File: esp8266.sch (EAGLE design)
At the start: 31 parts, among them U1 FT232RL-BASICSSOP, U2 SPX3819M5-L33, U3 SPX3819M5-L33

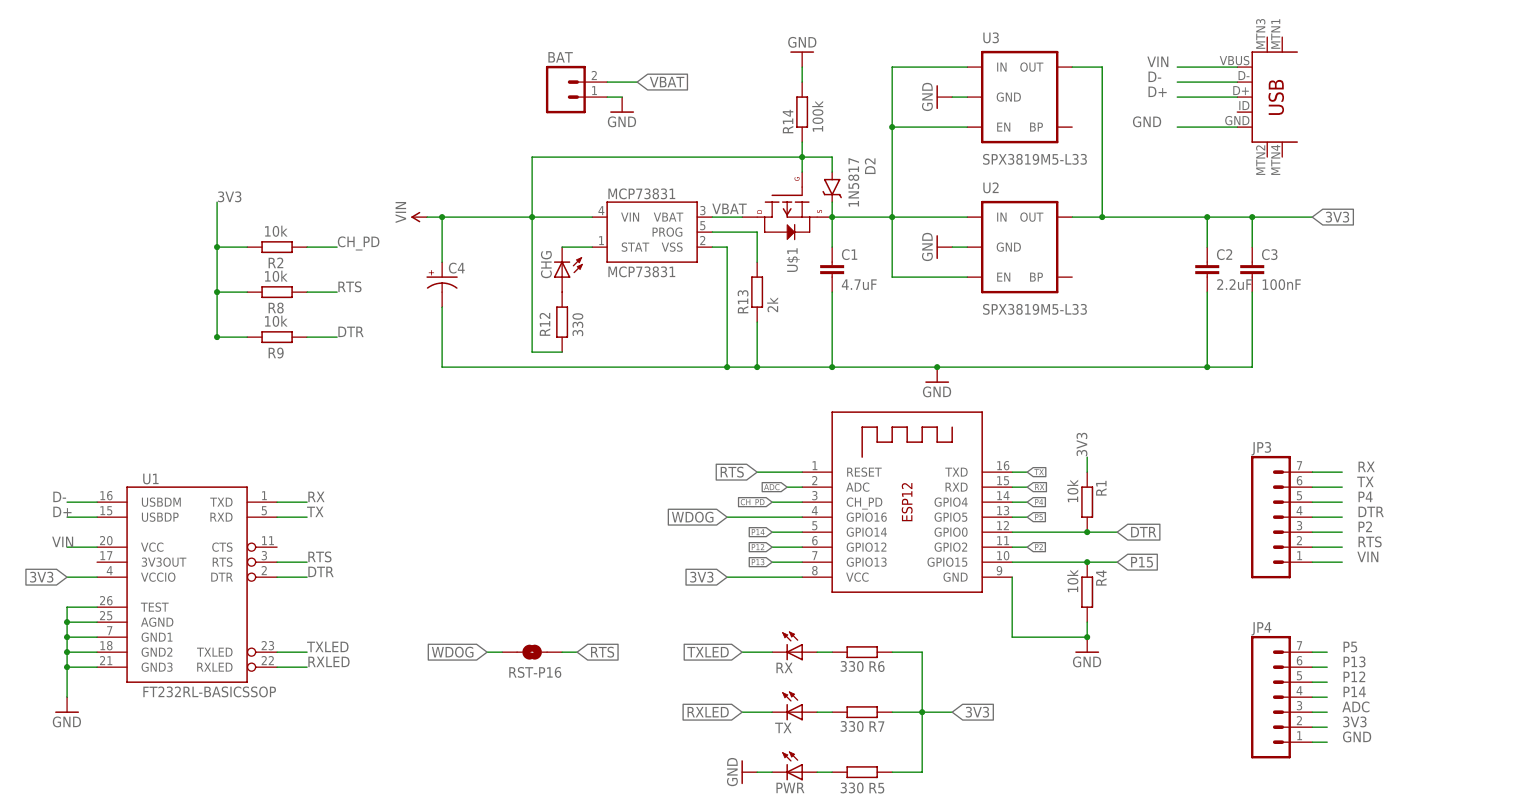
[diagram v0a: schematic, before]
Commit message: Minor fixes and improvements.
Watchdog with pull ups and a AND Gate;
Diode after VIN for satefy reasons;
Additional VIN pin on the other side of the board for completeness;
Switched order of pins 13 and 12;
Small border test holes for VIN and GND.
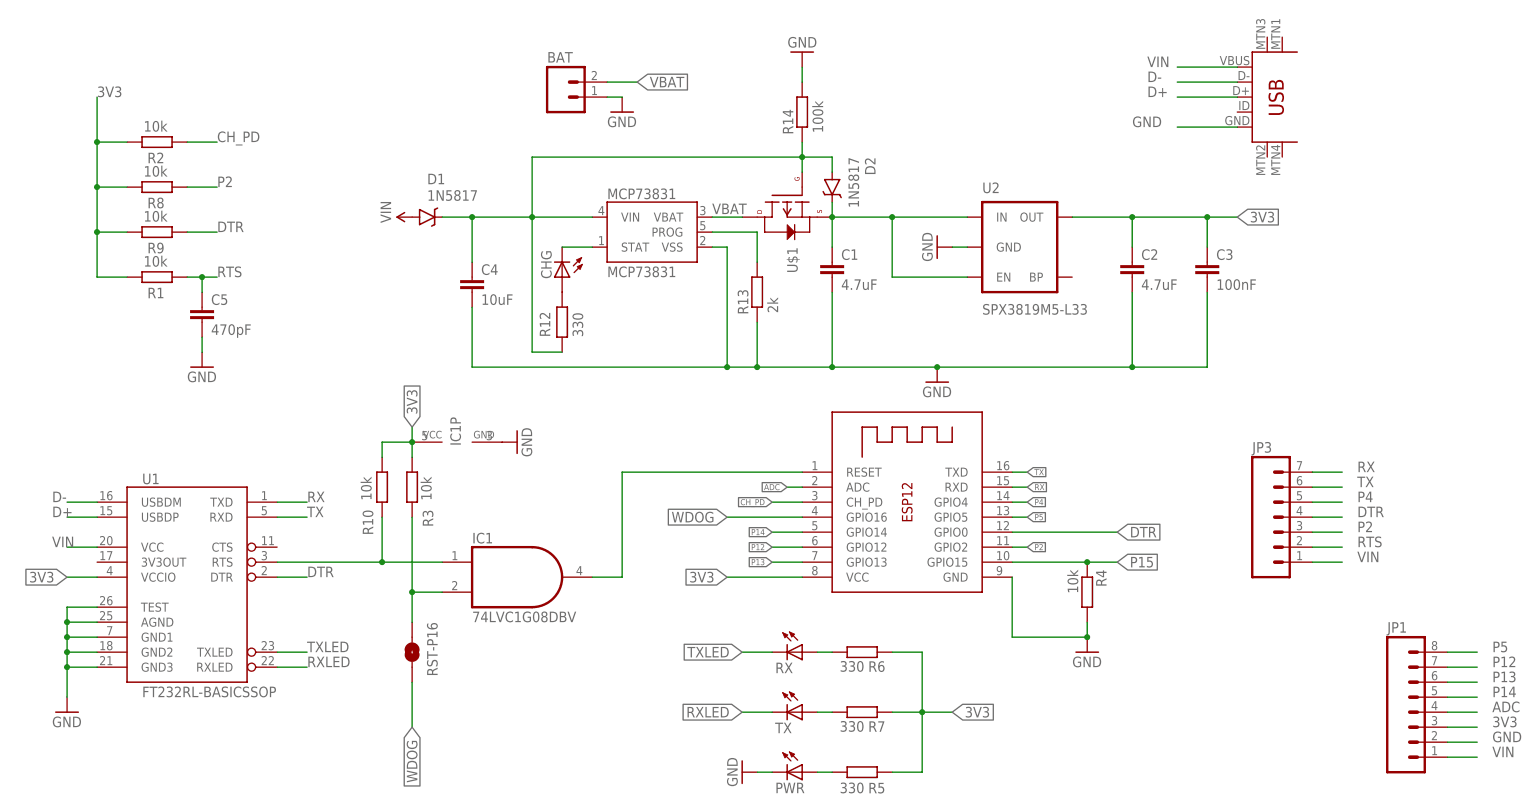
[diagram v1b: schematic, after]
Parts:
- removed JP4: (no value), SparkFun-Connectors:M07LOCK
- removed U3: SPX3819M5-L33, SparkFun-PowerIC:V_REG_LDOSMD
- added C5: 470pF, rcl:C-EUC0805
- added D1: 1N5817, SparkFun-DiscreteSemi:DIODE-SCHOTTKY-MBRA140
- added IC1: 74LVC1G08DBV, 74xx-little-us:74LVC1G08DBV
- added JP1: (no value), SparkFun-Connectors:M08LOCK
- added R10, R3: 10k, resistor:R-EU_R0805
- C2: value 2.2uF -> 4.7uF
- C4: value (none) -> 10uF; device SparkFun-Capacitors:CAP_POL1206 -> rcl:C-EUC0805
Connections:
- new net FTDI_RTS: IC1A.I0, R10.1, U1.RTS
- new net N$2: C4.1, D1.C, D2.A, MCP73831.VIN, R12.1, R14.1, U$1.G
- new net N$4: IC1A.I1, R3.1, RST-P16.1
- net 3V3: now also IC1P.VCC, JP1.3, R10.2, R3.2; no longer JP4.2, U3.OUT
- net ADC: now also JP1.4; no longer JP4.3
- net DTR: no longer R1.2
- net GND: now also C4.2, C5.2, IC1P.GND, JP1.2; no longer C4.-, JP4.1, U3.GND
- net P12: now also JP1.7; no longer JP4.5
- net P13: now also JP1.6; no longer JP4.6
- net P14: now also JP1.5; no longer JP4.4
- net P2: now also R8.2
- net P5: now also JP1.8; no longer JP4.7
- net RTS: now also C5.1, IC1A.O, R1.2; no longer R8.2, RST-P16.1, U1.RTS
- net VIN: now also D1.A, JP1.1; no longer C4.+, D2.A, MCP73831.VIN, R12.1, R14.1, U$1.G
- net VRIN: no longer U3.EN, U3.IN
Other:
- moved on the sheet: C2, C3, R1, R2, R8, R9, RST-P16

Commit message: Remove unnecessary components
RTS had a capacitor that is not required per FTDI spec and is also not needed for this
circuit. There were also 2 10k pull-ups on the RTS.
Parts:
- removed C5: 470pF, rcl:C-EUC0805
- removed R1: 10k, resistor:R-EU_R0805
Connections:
- net 3V3: no longer R1.1
- net GND: no longer C5.2
- net RTS: no longer C5.1, R1.2
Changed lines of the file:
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@@
 <part name="U2" library="SparkFun-PowerIC" deviceset="V_REG_LDO" device="SMD" value="SPX3819M5-L33"/>
 <part name="GND1" library="supply1" deviceset="GND" device=""/>
-<part name="R1" library="resistor" deviceset="R-EU_" device="R0805" value="10k"/>
-<part name="C5" library="rcl" deviceset="C-EU" device="C0805" value="470pF"/>
-<part name="GND9" library="supply1" deviceset="GND" device=""/>
 <part name="C4" library="rcl" deviceset="C-EU" device="C0805" value="10uF"/>
 <part name="D1" library="SparkFun-DiscreteSemi" deviceset="DIODE-SCHOTTKY" device="-MBRA140" value="1N5817"/>
@@
 </instance>
 <instance part="GND1" gate="1" x="27.94" y="109.22" rot="R270"/>
-<instance part="R1" gate="G$1" x="-104.14" y="104.14" smashed="yes">
-<attribute name="NAME" x="-102.87" y="102.3366" size="1.778" layer="95" rot="R180"/>
-<attribute name="VALUE" x="-102.362" y="107.696" size="1.778" layer="96" rot="R180"/>
-</instance>
-<instance part="C5" gate="G$1" x="-96.52" y="99.06"/>
-<instance part="GND9" gate="1" x="-96.52" y="88.9"/>
 <instance part="C4" gate="G$1" x="-50.8" y="104.14"/>
 <instance part="D1" gate="G$1" x="-58.42" y="114.3" smashed="yes">
@@
 </segment>
 <segment>
-<pinref part="C5" gate="G$1" pin="2"/>
-<wire x1="-96.52" y1="93.98" x2="-96.52" y2="91.44" width="0.1524" layer="91"/>
-<pinref part="GND9" gate="1" pin="GND"/>
-</segment>
-<segment>
 <pinref part="JP1" gate="G$1" pin="2"/>
 <wire x1="114.3" y1="25.4" x2="119.38" y2="25.4" width="0.1524" layer="91"/>
@@
 <wire x1="91.44" y1="58.42" x2="96.52" y2="58.42" width="0.1524" layer="91"/>
 <label x="99.06" y="58.42" size="1.778" layer="95"/>
-</segment>
-<segment>
-<pinref part="R1" gate="G$1" pin="2"/>
-<wire x1="-99.06" y1="104.14" x2="-96.52" y2="104.14" width="0.1524" layer="91"/>
-<label x="-93.98" y="104.14" size="1.778" layer="95"/>
-<pinref part="C5" gate="G$1" pin="1"/>
-<wire x1="-96.52" y1="104.14" x2="-93.98" y2="104.14" width="0.1524" layer="91"/>
-<wire x1="-96.52" y1="101.6" x2="-96.52" y2="104.14" width="0.1524" layer="91"/>
-<junction x="-96.52" y="104.14"/>
 </segment>
 </net>
@@
 <junction x="-114.3" y="127"/>
 <junction x="-114.3" y="119.38"/>
-<junction x="-114.3" y="111.76"/>
-<pinref part="R1" gate="G$1" pin="1"/>
-<wire x1="-109.22" y1="104.14" x2="-114.3" y2="104.14" width="0.1524" layer="91"/>
-<wire x1="-114.3" y1="104.14" x2="-114.3" y2="111.76" width="0.1524" layer="91"/>
-</segment>
-<segment>
+</segment>
+<segment>

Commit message: Change the second VIN to ground
It's more useful that way.
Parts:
- added PFET2: BSS84, transistor-small-signal:BSS84
- renumbered U$1 to PFET1
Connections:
- new net N$5: BAT.1, PFET2.D
- net GND: now also BAT.2, JP3.1, PFET2.G; no longer BAT.1
- net VBAT: now also PFET2.S; no longer BAT.2
- net VIN: no longer JP3.1
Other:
- moved on the sheet: BAT
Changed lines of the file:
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@@
 <?xml version="1.0" encoding="utf-8"?>
 <!DOCTYPE eagle SYSTEM "eagle.dtd">
-<eagle version="7.3.0">
+<eagle version="7.4.0">
 <drawing>
 <settings>
@@
 <part name="BAT" library="SparkFun-Connectors" deviceset="M02" device="LOCK"/>
 <part name="SUPPLY1" library="SparkFun-Aesthetics" deviceset="VIN" device=""/>
-<part name="GND4" library="supply1" deviceset="GND" device=""/>
-<part name="U$1" library="GeekAmmo" deviceset="P-CHANNEL-MOSFET" device=""/>
+<part name="PFET1" library="GeekAmmo" deviceset="P-CHANNEL-MOSFET" device=""/>
 <part name="R14" library="resistor" deviceset="R-EU_" device="R0805" value="100k"/>
 <part name="GND6" library="supply1" deviceset="GND" device=""/>
@@
 <part name="JP1" library="SparkFun-Connectors" deviceset="M08" device="LOCK"/>
 <part name="GND7" library="supply1" deviceset="GND" device=""/>
+<part name="PFET2" library="transistor-small-signal" deviceset="BSS84" device=""/>
+<part name="GND4" library="supply1" deviceset="GND" device=""/>
 </parts>
 <sheets>
@@
 <attribute name="VALUE" x="1.016" y="98.044" size="1.778" layer="96" rot="R90"/>
 </instance>
-<instance part="BAT" gate="G$1" x="-35.56" y="134.62"/>
+<instance part="BAT" gate="G$1" x="-48.26" y="137.16"/>
 <instance part="SUPPLY1" gate="G$1" x="-60.96" y="114.3" rot="R90"/>
-<instance part="GND4" gate="1" x="-25.4" y="132.08"/>
-<instance part="U$1" gate="G$1" x="2.54" y="116.84" smashed="yes" rot="R270">
+<instance part="PFET1" gate="G$1" x="2.54" y="116.84" smashed="yes" rot="R270">
 <attribute name="NAME" x="2.54" y="109.22" size="1.778" layer="95" rot="R270"/>
 </instance>
@@
 <instance part="IC1" gate="P" x="-53.34" y="76.2" rot="R90"/>
 <instance part="GND7" gate="1" x="-43.18" y="76.2" rot="R90"/>
+<instance part="PFET2" gate="G$1" x="-30.48" y="137.16" rot="R270"/>
+<instance part="GND4" gate="1" x="-27.94" y="144.78" rot="R180"/>
 </instances>
 <busses>
@@
 </segment>
 <segment>
-<pinref part="BAT" gate="G$1" pin="1"/>
-<wire x1="-25.4" y1="134.62" x2="-27.94" y2="134.62" width="0.1524" layer="91"/>
-<pinref part="GND4" gate="1" pin="GND"/>
-</segment>
-<segment>
 <pinref part="GND6" gate="1" pin="GND"/>
 <pinref part="R14" gate="G$1" pin="2"/>
@@
 <pinref part="GND7" gate="1" pin="GND"/>
 </segment>
+<segment>
+<pinref part="BAT" gate="G$1" pin="2"/>
+<pinref part="GND4" gate="1" pin="GND"/>
+<pinref part="PFET2" gate="G$1" pin="G"/>
+<junction x="-27.94" y="142.24"/>
+<wire x1="-40.64" y1="139.7" x2="-40.64" y2="142.24" width="0.1524" layer="91"/>
+<wire x1="-40.64" y1="142.24" x2="-27.94" y2="142.24" width="0.1524" layer="91"/>
+</segment>
+<segment>
+<pinref part="JP3" gate="G$1" pin="1"/>
+<wire x1="91.44" y1="55.88" x2="96.52" y2="55.88" width="0.1524" layer="91"/>
+<label x="99.06" y="55.88" size="1.778" layer="95"/>
+</segment>
 </net>
 <net name="P15" class="0">
@@
 <net name="VBAT" class="0">
 <segment>
-<pinref part="BAT" gate="G$1" pin="2"/>
-<wire x1="-27.94" y1="137.16" x2="-22.86" y2="137.16" width="0.1524" layer="91"/>
-<label x="-22.86" y="137.16" size="1.778" layer="95" xref="yes"/>
+<label x="-17.78" y="137.16" size="1.778" layer="95" xref="yes"/>
+<pinref part="PFET2" gate="G$1" pin="S"/>
+<wire x1="-25.4" y1="137.16" x2="-17.78" y2="137.16" width="0.1524" layer="91"/>
 </segment>
 <segment>
 <pinref part="MCP73831" gate="G$1" pin="VBAT"/>
-<pinref part="U$1" gate="G$1" pin="D"/>
+<pinref part="PFET1" gate="G$1" pin="D"/>
 <wire x1="-10.16" y1="114.3" x2="-5.08" y2="114.3" width="0.1524" layer="91"/>
 <label x="-10.16" y="114.808" size="1.778" layer="95"/>
@@
 </net>
 <net name="VIN" class="1">
-<segment>
-<pinref part="JP3" gate="G$1" pin="1"/>
-<wire x1="91.44" y1="55.88" x2="96.52" y2="55.88" width="0.1524" layer="91"/>
-<label x="99.06" y="55.88" size="1.778" layer="95"/>
-</segment>
 <segment>
 <pinref part="MINIUSB" gate="G$1" pin="VBUS"/>
@@
 <net name="VRIN" class="1">
 <segment>
-<pinref part="U$1" gate="G$1" pin="S"/>
+<pinref part="PFET1" gate="G$1" pin="S"/>
 <pinref part="C1" gate="G$1" pin="1"/>
 <wire x1="10.16" y1="109.22" x2="10.16" y2="114.3" width="0.1524" layer="91"/>
@@
 <wire x1="-40.64" y1="114.3" x2="-40.64" y2="124.46" width="0.1524" layer="91"/>
 <wire x1="-40.64" y1="124.46" x2="5.08" y2="124.46" width="0.1524" layer="91"/>
-<pinref part="U$1" gate="G$1" pin="G"/>
+<pinref part="PFET1" gate="G$1" pin="G"/>
 <wire x1="5.08" y1="121.92" x2="5.08" y2="124.46" width="0.1524" layer="91"/>
 <wire x1="5.08" y1="124.46" x2="10.16" y2="124.46" width="0.1524" layer="91"/>
@@
 </segment>
 </net>
+<net name="N$5" class="0">
+<segment>
+<pinref part="BAT" gate="G$1" pin="1"/>
+<pinref part="PFET2" gate="G$1" pin="D"/>
+<wire x1="-35.56" y1="137.16" x2="-40.64" y2="137.16" width="0.1524" layer="91"/>
+</segment>
+</net>

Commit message: More clearance adjustments and labeling improvements
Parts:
- renumbered IC1 to AND, U2 to SPX
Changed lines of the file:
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@@
 <part name="GND8" library="supply1" deviceset="GND" device=""/>
 <part name="D2" library="SparkFun-DiscreteSemi" deviceset="DIODE-SCHOTTKY" device="-MBRA140" value="1N5817"/>
-<part name="U2" library="SparkFun-PowerIC" deviceset="V_REG_LDO" device="SMD" value="SPX3819M5-L33"/>
+<part name="SPX" library="SparkFun-PowerIC" deviceset="V_REG_LDO" device="SMD" value="SPX3819M5-L33"/>
 <part name="GND1" library="supply1" deviceset="GND" device=""/>
 <part name="C4" library="rcl" deviceset="C-EU" device="C0805" value="10uF"/>
 <part name="D1" library="SparkFun-DiscreteSemi" deviceset="DIODE-SCHOTTKY" device="-MBRA140" value="1N5817"/>
-<part name="IC1" library="74xx-little-us" deviceset="74*1G08" device="DBV" technology="LVC"/>
+<part name="AND" library="74xx-little-us" deviceset="74*1G08" device="DBV" technology="LVC"/>
 <part name="R3" library="resistor" deviceset="R-EU_" device="R0805" value="10k"/>
 <part name="R10" library="resistor" deviceset="R-EU_" device="R0805" value="10k"/>
@@
 <attribute name="VALUE" x="12.9286" y="124.46" size="1.778" layer="96" rot="R270"/>
 </instance>
-<instance part="U2" gate="G$1" x="43.18" y="109.22" smashed="yes">
+<instance part="SPX" gate="G$1" x="43.18" y="109.22" smashed="yes">
 <attribute name="NAME" x="35.56" y="118.364" size="1.778" layer="95"/>
 <attribute name="VALUE" x="35.56" y="97.79" size="1.778" layer="96"/>
@@
 <attribute name="VALUE" x="-58.42" y="117.0686" size="1.778" layer="96"/>
 </instance>
-<instance part="IC1" gate="A" x="-43.18" y="53.34"/>
+<instance part="AND" gate="A" x="-43.18" y="53.34"/>
 <instance part="R3" gate="G$1" x="-60.96" y="68.58" smashed="yes" rot="R90">
 <attribute name="NAME" x="-59.1566" y="64.77" size="1.778" layer="95" rot="R270"/>
@@
 </instance>
 <instance part="JP1" gate="G$1" x="109.22" y="30.48"/>
-<instance part="IC1" gate="P" x="-53.34" y="76.2" rot="R90"/>
+<instance part="AND" gate="P" x="-53.34" y="76.2" rot="R90"/>
 <instance part="GND7" gate="1" x="-43.18" y="76.2" rot="R90"/>
 <instance part="PFET2" gate="G$1" x="-30.48" y="137.16" rot="R270"/>
@@
 <segment>
 <pinref part="GND1" gate="1" pin="GND"/>
-<pinref part="U2" gate="G$1" pin="GND"/>
+<pinref part="SPX" gate="G$1" pin="GND"/>
 <wire x1="30.48" y1="109.22" x2="33.02" y2="109.22" width="0.1524" layer="91"/>
 </segment>
@@
 </segment>
 <segment>
-<pinref part="IC1" gate="P" pin="GND"/>
+<pinref part="AND" gate="P" pin="GND"/>
 <pinref part="GND7" gate="1" pin="GND"/>
 </segment>
@@
 <segment>
 <pinref part="ESP8266-07/12" gate="G$1" pin="RESET"/>
-<pinref part="IC1" gate="A" pin="O"/>
+<pinref part="AND" gate="A" pin="O"/>
 <wire x1="-30.48" y1="53.34" x2="-25.4" y2="53.34" width="0.1524" layer="91"/>
 <wire x1="-25.4" y1="53.34" x2="-25.4" y2="71.12" width="0.1524" layer="91"/>
@@
 <junction x="10.16" y="114.3"/>
 <pinref part="D2" gate="G$1" pin="C"/>
-<pinref part="U2" gate="G$1" pin="IN"/>
+<pinref part="SPX" gate="G$1" pin="IN"/>
 <wire x1="10.16" y1="114.3" x2="20.32" y2="114.3" width="0.1524" layer="91"/>
 <wire x1="20.32" y1="114.3" x2="33.02" y2="114.3" width="0.1524" layer="91"/>
 <wire x1="20.32" y1="104.14" x2="20.32" y2="114.3" width="0.1524" layer="91"/>
 <junction x="20.32" y="114.3"/>
-<pinref part="U2" gate="G$1" pin="EN"/>
+<pinref part="SPX" gate="G$1" pin="EN"/>
 <wire x1="33.02" y1="104.14" x2="20.32" y2="104.14" width="0.1524" layer="91"/>
 </segment>
@@
 <wire x1="73.66" y1="109.22" x2="73.66" y2="114.3" width="0.1524" layer="91"/>
 <junction x="73.66" y="114.3"/>
-<pinref part="U2" gate="G$1" pin="OUT"/>
+<pinref part="SPX" gate="G$1" pin="OUT"/>
 <junction x="60.96" y="114.3"/>
 <wire x1="50.8" y1="114.3" x2="60.96" y2="114.3" width="0.1524" layer="91"/>
@@
 <junction x="-60.96" y="76.2"/>
 <label x="-60.96" y="78.74" size="1.778" layer="95" rot="R90" xref="yes"/>
-<pinref part="IC1" gate="P" pin="VCC"/>
+<pinref part="AND" gate="P" pin="VCC"/>
 </segment>
 <segment>
@@
 <segment>
 <pinref part="U1" gate="G$1" pin="RTS"/>
-<pinref part="IC1" gate="A" pin="I0"/>
+<pinref part="AND" gate="A" pin="I0"/>
 <wire x1="-83.82" y1="55.88" x2="-66.04" y2="55.88" width="0.1524" layer="91"/>
 <wire x1="-66.04" y1="55.88" x2="-55.88" y2="55.88" width="0.1524" layer="91"/>
@@
 <pinref part="RST-P16" gate="1" pin="1"/>
 <wire x1="-60.96" y1="45.72" x2="-60.96" y2="50.8" width="0.1524" layer="91"/>
-<pinref part="IC1" gate="A" pin="I1"/>
+<pinref part="AND" gate="A" pin="I1"/>
 <wire x1="-60.96" y1="50.8" x2="-55.88" y2="50.8" width="0.1524" layer="91"/>
 <wire x1="-60.96" y1="50.8" x2="-60.96" y2="63.5" width="0.1524" layer="91"/>
